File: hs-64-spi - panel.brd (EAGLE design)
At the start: 83 x 90.2 mm, 228 parts, among them J1 DF40C-70DP-0.4V(51), J10 A79622-001, J11 DF40C-70DP-0.4V(51), J12 A79622-001, J13 DF40C-70DP-0.4V(51), J14 A79622-001, J15 DF40C-70DP-0.4V(51), J16 A79622-001, J17 DF40C-70DP-0.4V(51), J18 A79622-001, J2 A79622-001, J3 DF40C-70DP-0.4V(51), J4 A79622-001, J5 DF40C-70DP-0.4V(51), J6 A79622-001, J7 DF40C-70DP-0.4V(51), J8 A79622-001, J9 DF40C-70DP-0.4V(51), U1 RHD2064_BGA, U10 ADXL335_IDAX, U11 RHD2064_BGA, U12 ADXL335_IDAX, U13 RHD2064_BGA, U14 ADXL335_IDAX, U15 RHD2064_BGA, U16 ADXL335_IDAX, U17 RHD2064_BGA, U18 ADXL335_IDAX, U2 ADXL335_IDAX, U3 RHD2064_BGA, U4 ADXL335_IDAX, U5 RHD2064_BGA, U6 ADXL335_IDAX, U7 RHD2064_BGA, U8 ADXL335_IDAX, U9 RHD2064_BGA, X1 OE-LOGO_3.5X2.5, X2 OE-LOGO_3.5X2.5, X3 OE-LOGO_3.5X2.5, X4 OE-LOGO_3.5X2.5, X5 OE-LOGO_3.5X2.5, X6 OE-LOGO_3.5X2.5, X7 OE-LOGO_3.5X2.5, X8 OE-LOGO_3.5X2.5

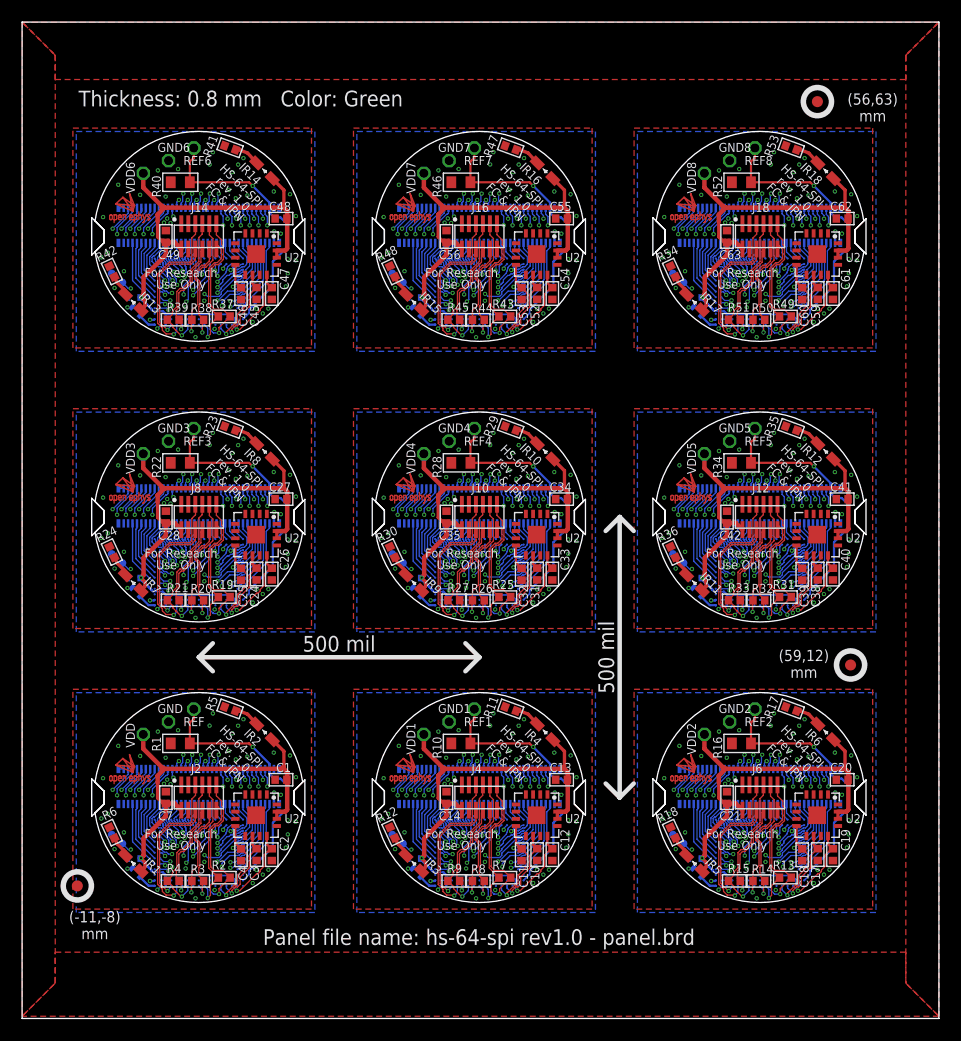
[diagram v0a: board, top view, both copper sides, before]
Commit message: Added PCB design files for the new version 1.1.
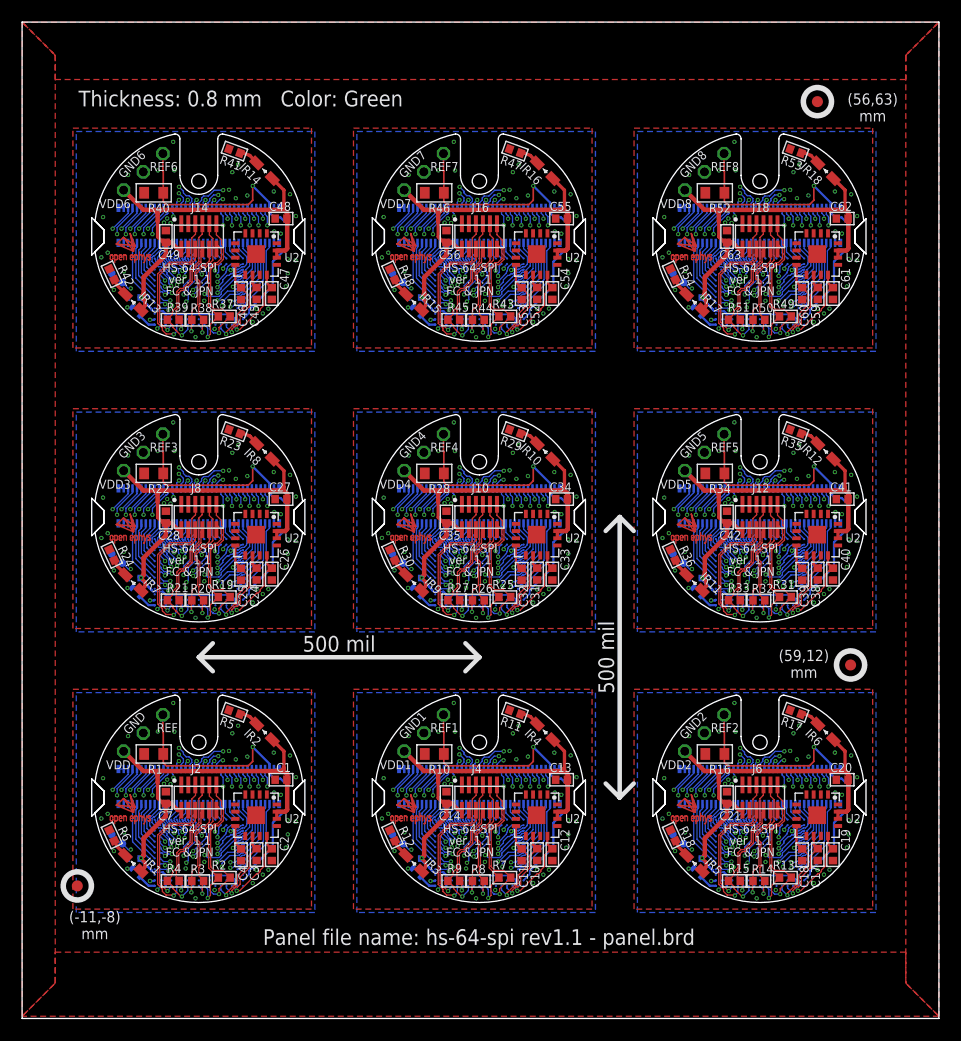
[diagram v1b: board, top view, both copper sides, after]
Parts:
- C1, C13, C20, C27, C34, C41, C48, C55, C62: value 100n -> 0.1uF
- R11, R12, R17, R18, R23, R24, R29, R30, R35, R36, R41, R42, R47, R48, R5, R53, R54, R6: value 100 -> 820
- moved X 3.63 mm to (-6.37, -1.44)
- moved X1 3.63 mm to (19.0, -1.44)
- moved X2 3.63 mm to (44.4, -1.44)
- moved X3 3.63 mm to (-6.37, 24.0)
- moved X4 3.63 mm to (19.0, 24.0)
- moved X5 3.63 mm to (44.4, 24.0)
- moved X6 3.63 mm to (-6.37, 49.4)
- moved X7 3.63 mm to (19.0, 49.4)
- moved X8 3.63 mm to (44.4, 49.4)
- moved REF3 2.84 mm to (-3.25, 32.9)
- moved REF6 2.84 mm to (-3.25, 58.3)
- moved REF 2.84 mm to (-3.25, 7.49)
- moved REF4 2.84 mm to (22.1, 32.9)
- moved REF5 2.84 mm to (47.5, 32.9)
- moved REF7 2.84 mm to (22.1, 58.3)
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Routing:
- net REF8: track 24.4 -> 29.3 mm
- net REF2: track 24.4 -> 29.3 mm
- net REF5: track 24.4 -> 29.3 mm
- net REF7: track 24.4 -> 29.3 mm
- net REF6: track 24.4 -> 29.3 mm
- net REF1: track 24.4 -> 29.3 mm
- net REF: track 24.4 -> 29.3 mm
- net REF4: track 24.4 -> 29.3 mm
- net REF3: track 24.4 -> 29.3 mm
- net E351: track 9.77 -> 13.5 mm
- net E223: track 9.77 -> 13.5 mm
- net E95: track 9.77 -> 13.5 mm
- net E287: track 9.77 -> 13.5 mm
- net E159: track 9.77 -> 13.5 mm
- net E31: track 9.77 -> 13.5 mm
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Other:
- outline, holes or cut-outs redrawn
- board text added: "HS-64-SPI ver. 1.1 FC & JPN"
- board text added: "Panel file name: hs-64-spi rev1.1 - panel.brd"
- board text removed: "HS-64-SPI rev. 1.0 FC & JPN"
- board text removed: "Panel file name: hs-64-spi rev1.0 - panel.brd"
- board text removed: "www.open-ephys.org"

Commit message: Added fiducials on bottom.
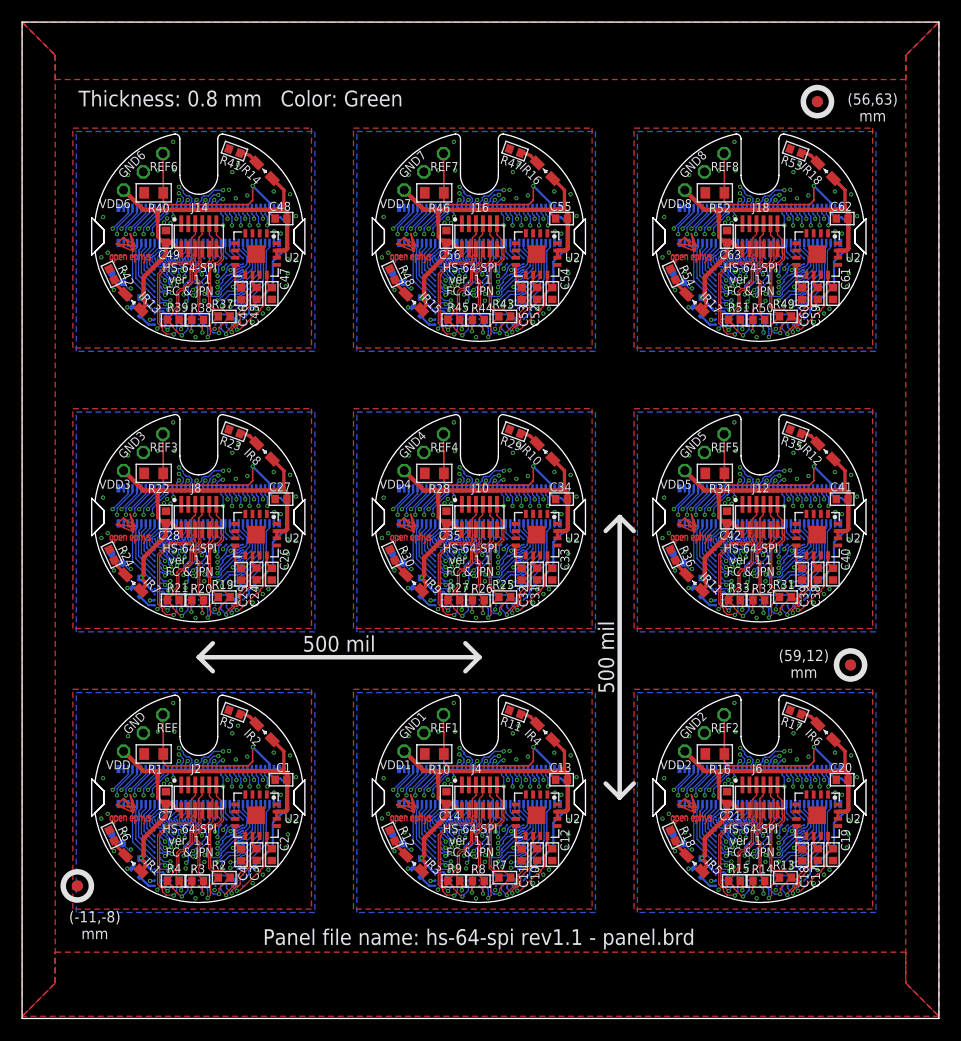
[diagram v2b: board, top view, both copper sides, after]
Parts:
- added E$4, E$5, E$6: (no value), fiducial:FIDUCIAL
